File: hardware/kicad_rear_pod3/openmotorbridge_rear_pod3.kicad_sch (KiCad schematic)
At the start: 4 parts, among them J1 M8_3PIN_SOCKET, U1 ESP32-C3-WROOM-02, U2 MAX-M10S, U3 SX1262

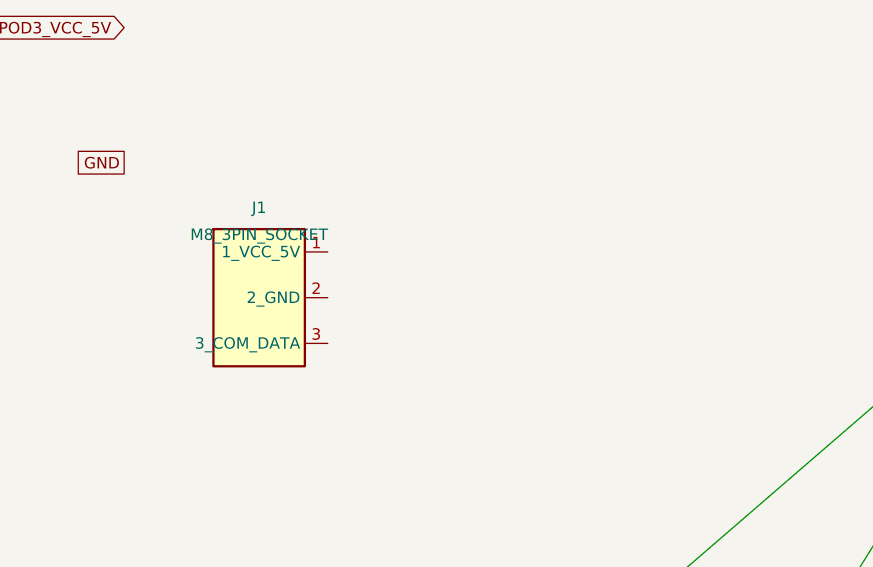
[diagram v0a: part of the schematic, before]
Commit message: feat(hardware,firmware): integrate OMM UART push flashing, low-profile cartridge & pod3 6-pin layout
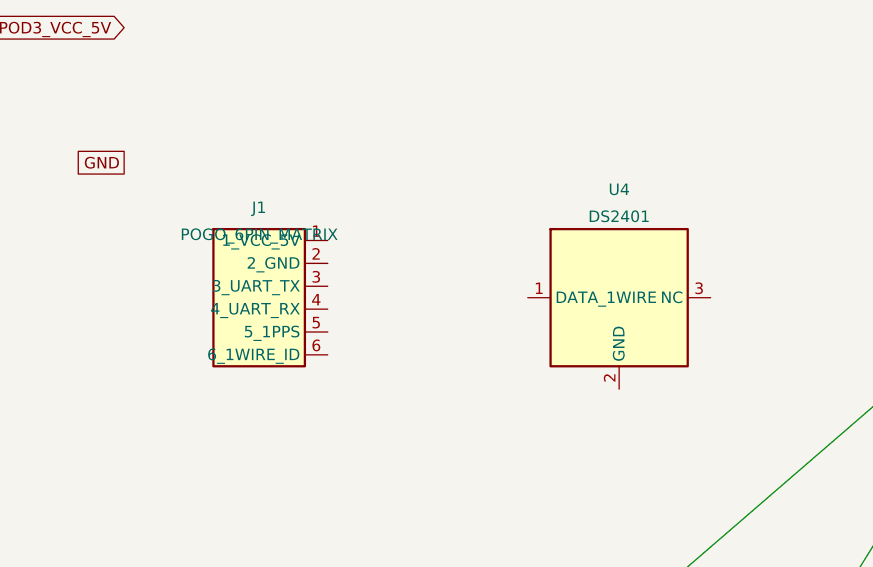
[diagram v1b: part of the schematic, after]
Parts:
- added U4: DS2401, symbol Memory_EEPROM:DS2401P
- J1: value M8_3PIN_SOCKET -> POGO_6PIN_MATRIX; symbol Connector:M8_3Pin -> Connector:Conn_01x06
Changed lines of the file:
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@@
 	(global_label "GNSS_1PPS" (shape output) (at 250.0 60.0 0) (effects (font (size 1.27 1.27)) (justify left)))
 	(global_label "POD3_1WIRE_ID" (shape bidirectional) (at 250.0 70.0 0) (effects (font (size 1.27 1.27)) (justify left)))
-	(symbol (lib_id "Connector:M8_3Pin") (at 45.0 70.0 0) (unit 1)
+	(symbol (lib_id "Connector:Conn_01x06") (at 45.0 70.0 0) (unit 1)
 		(in_bom yes) (on_board yes) (dnp no)
 		(property "Reference" "J1" (at 45.0 60.0 0) (effects (font (size 1.27 1.27))))
-		(property "Value" "M8_3PIN_SOCKET" (at 45.0 63.0 0) (effects (font (size 1.27 1.27))))
+		(property "Value" "POGO_6PIN_MATRIX" (at 45.0 63.0 0) (effects (font (size 1.27 1.27))))
 		(pin "1")
 		(pin "2")
+		(pin "3")
+		(pin "4")
+		(pin "5")
+		(pin "6")
+	)
+	(symbol (lib_id "Memory_EEPROM:DS2401P") (at 85.0 70.0 0) (unit 1)
+		(in_bom yes) (on_board yes) (dnp no)
+		(property "Reference" "U4" (at 85.0 58.0 0) (effects (font (size 1.27 1.27))))
+		(property "Value" "DS2401" (at 85.0 61.0 0) (effects (font (size 1.27 1.27))))
+		(pin "1")
+		(pin "2")

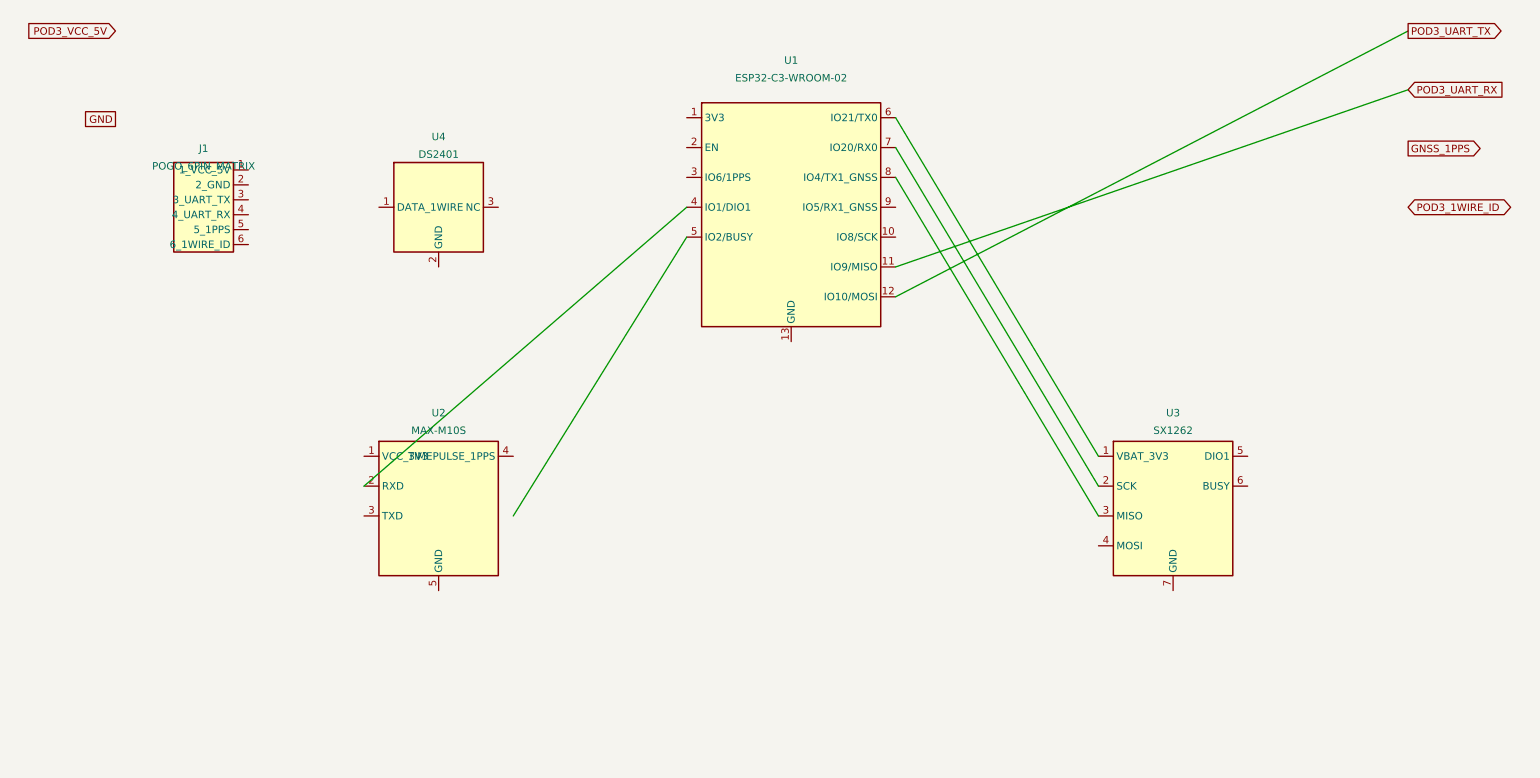
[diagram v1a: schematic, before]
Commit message: feat(hardware): finalize Pod 3 PCB routing, 110x52mm enclosure, 3x MM8030 RF switches, and manufacturing packages
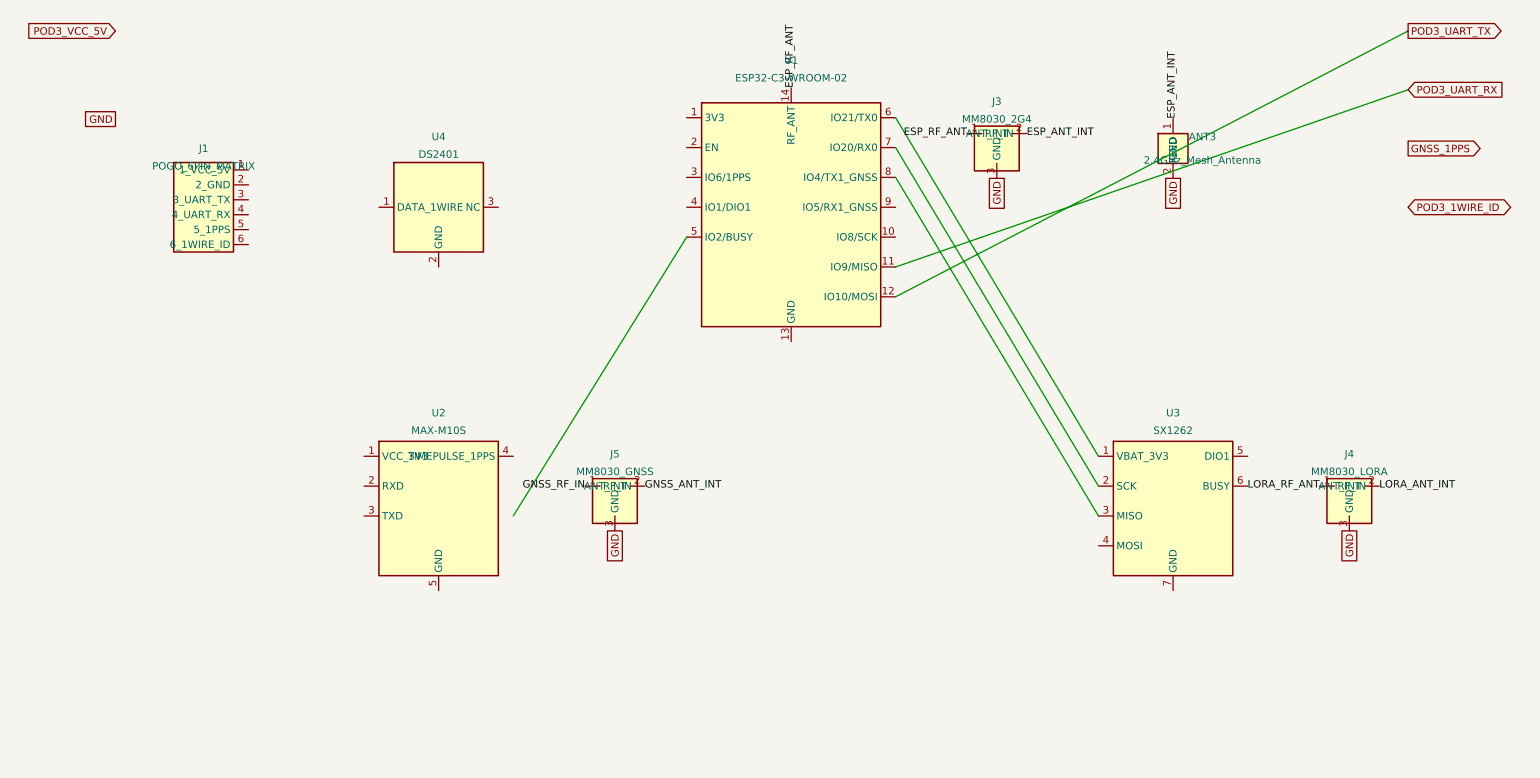
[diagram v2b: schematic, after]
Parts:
- added ANT3: 2.4GHz_Mesh_Antenna, symbol RF_Antenna:Pulse_W3000
- added J3: MM8030_2G4, symbol Connector_Coaxial:Murata_MM8030
- added J4: MM8030_LORA, symbol Connector_Coaxial:Murata_MM8030
- added J5: MM8030_GNSS, symbol Connector_Coaxial:Murata_MM8030
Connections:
- net GND: now also ANT3.2 (GND), J3.3 (GND), J4.3 (GND), J5.3 (GND)
- net at U2.2 (RXD): no longer U1.4 (IO1/DIO1)
- new net ESP_ANT_INT: ANT3.1 (FEED), J3.2 (ANT_INT)
- new net ESP_RF_ANT: J3.1 (RF_IN), U1.14 (RF_ANT)
- new net GNSS_ANT_INT: J5.2 (ANT_INT)
- new net GNSS_RF_IN: J5.1 (RF_IN)
- new net LORA_ANT_INT: J4.2 (ANT_INT)
- new net LORA_RF_ANT: J4.1 (RF_IN)
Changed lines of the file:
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@@
 		(pin "12")
 		(pin "13")
+		(pin "14")
 	)
+	(label "ESP_RF_ANT" (at 145.0 49.68 90) (effects (font (size 1.27 1.27))))
 	(symbol (lib_id "RF_Transceiver:SX1262") (at 210.0 120.0 0) (unit 1)
 		(in_bom yes) (on_board yes) (dnp no)
@@
 	(wire (pts (xy 162.78 54.76) (xy 197.3 112.38)) (stroke (width 0) (type solid)))
 	(wire (pts (xy 97.7 122.54) (xy 127.22 75.08)) (stroke (width 0) (type solid)))
-	(wire (pts (xy 72.3 117.46) (xy 127.22 70.0)) (stroke (width 0) (type solid)))
+	(symbol (lib_id "Connector_Coaxial:Murata_MM8030") (at 180.0 60.0 0) (unit 1)
+		(in_bom yes) (on_board yes) (dnp no)
+		(property "Reference" "J3" (at 180.0 52.0 0) (effects (font (size 1.27 1.27))))
+		(property "Value" "MM8030_2G4" (at 180.0 55.0 0) (effects (font (size 1.27 1.27))))
+		(pin "1")
+		(pin "2")
+		(pin "3")
+	)
+	(label "ESP_RF_ANT" (at 174.92 57.46 180) (effects (font (size 1.27 1.27)) (justify right)))
+	(label "ESP_ANT_INT" (at 185.08 57.46 0) (effects (font (size 1.27 1.27)) (justify left)))
+	(global_label "GND" (shape passive) (at 180.0 65.08 270) (effects (font (size 1.27 1.27))))
+	(symbol (lib_id "Connector_Coaxial:Murata_MM8030") (at 240.0 120.0 0) (unit 1)
+		(in_bom yes) (on_board yes) (dnp no)
+		(property "Reference" "J4" (at 240.0 112.0 0) (effects (font (size 1.27 1.27))))
+		(property "Value" "MM8030_LORA" (at 240.0 115.0 0) (effects (font (size 1.27 1.27))))
+		(pin "1")
+		(pin "2")
+		(pin "3")
+	)
+	(label "LORA_RF_ANT" (at 234.92 117.46 180) (effects (font (size 1.27 1.27)) (justify right)))
+	(label "LORA_ANT_INT" (at 245.08 117.46 0) (effects (font (size 1.27 1.27)) (justify left)))
+	(global_label "GND" (shape passive) (at 240.0 125.08 270) (effects (font (size 1.27 1.27))))
+	(symbol (lib_id "Connector_Coaxial:Murata_MM8030") (at 115.0 120.0 0) (unit 1)
+		(in_bom yes) (on_board yes) (dnp no)
+		(property "Reference" "J5" (at 115.0 112.0 0) (effects (font (size 1.27 1.27))))
+		(property "Value" "MM8030_GNSS" (at 115.0 115.0 0) (effects (font (size 1.27 1.27))))
+		(pin "1")
+		(pin "2")
+		(pin "3")
+	)
+	(label "GNSS_RF_IN" (at 109.92 117.46 180) (effects (font (size 1.27 1.27)) (justify right)))
+	(label "GNSS_ANT_INT" (at 120.08 117.46 0) (effects (font (size 1.27 1.27)) (justify left)))
+	(global_label "GND" (shape passive) (at 115.0 125.08 270) (effects (font (size 1.27 1.27))))
+	(symbol (lib_id "RF_Antenna:Pulse_W3000") (at 210.0 60.0 0) (unit 1)
+		(in_bom yes) (on_board yes) (dnp no)
+		(property "Reference" "ANT3" (at 215.0 58.0 0) (effects (font (size 1.27 1.27))))
+		(property "Value" "2.4GHz_Mesh_Antenna" (at 215.0 62.0 0) (effects (font (size 1.27 1.27))))
+		(pin "1")
+		(pin "2")
+	)
+	(label "ESP_ANT_INT" (at 210.0 54.92 90) (effects (font (size 1.27 1.27)) (justify left)))
+	(global_label "GND" (shape passive) (at 210.0 65.08 270) (effects (font (size 1.27 1.27))))
 )

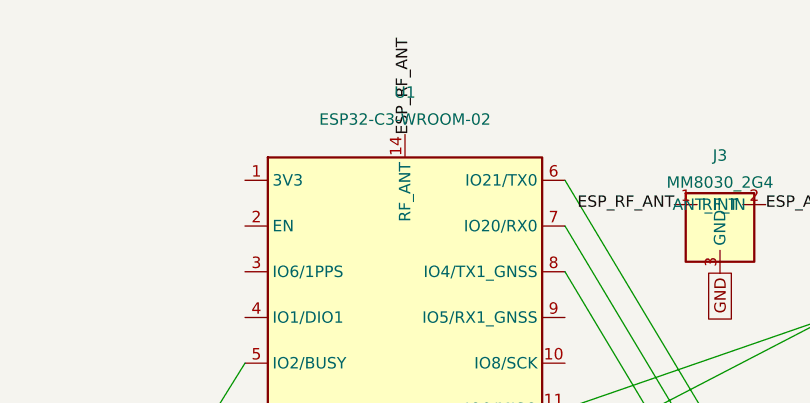
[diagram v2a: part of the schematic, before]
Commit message: feat(omm): adopt compact PCBA with modular antenna bracket and U.FL pigtails
- Updated Central Base Box to ESP32-S3-WROOM-1U (U.FL micro-coax to upper lid FPC)
- Reduced OMM PCBA to compact 55x48mm using ESP32-C3-WROOM-02U (U.FL)
- Added 2 extra M2 floor standoffs (X=50.5mm) to shared 00_base_sled.scad (100% universal across all pods)
- Created modular 04_antenna_bracket_omm.scad for rear chamber securing GPS patch, LoRa FPC, and SMA coax
- Re-compiled all 27 STLs and 11 CAD renders
- Regenerated JLCPCB manufacturing packages (Gerbers, BOM, CPL, ZIPs)
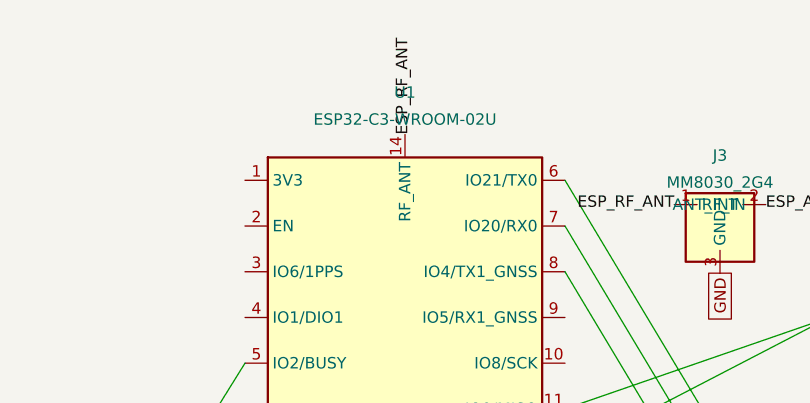
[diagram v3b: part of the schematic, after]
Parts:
- U1: value ESP32-C3-WROOM-02 -> ESP32-C3-WROOM-02U
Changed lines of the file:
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@@
 		(in_bom yes) (on_board yes) (dnp no)
 		(property "Reference" "U1" (at 145.0 45.0 0) (effects (font (size 1.27 1.27))))
-		(property "Value" "ESP32-C3-WROOM-02" (at 145.0 48.0 0) (effects (font (size 1.27 1.27))))
+		(property "Value" "ESP32-C3-WROOM-02U" (at 145.0 48.0 0) (effects (font (size 1.27 1.27))))
 		(pin "1")
 		(pin "2")
